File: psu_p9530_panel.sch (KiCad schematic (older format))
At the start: 66 parts, among them IC306 LTC1658, IC308 CD4052B, IC310 TLC272, IC312 TLC272, U401 54LS164

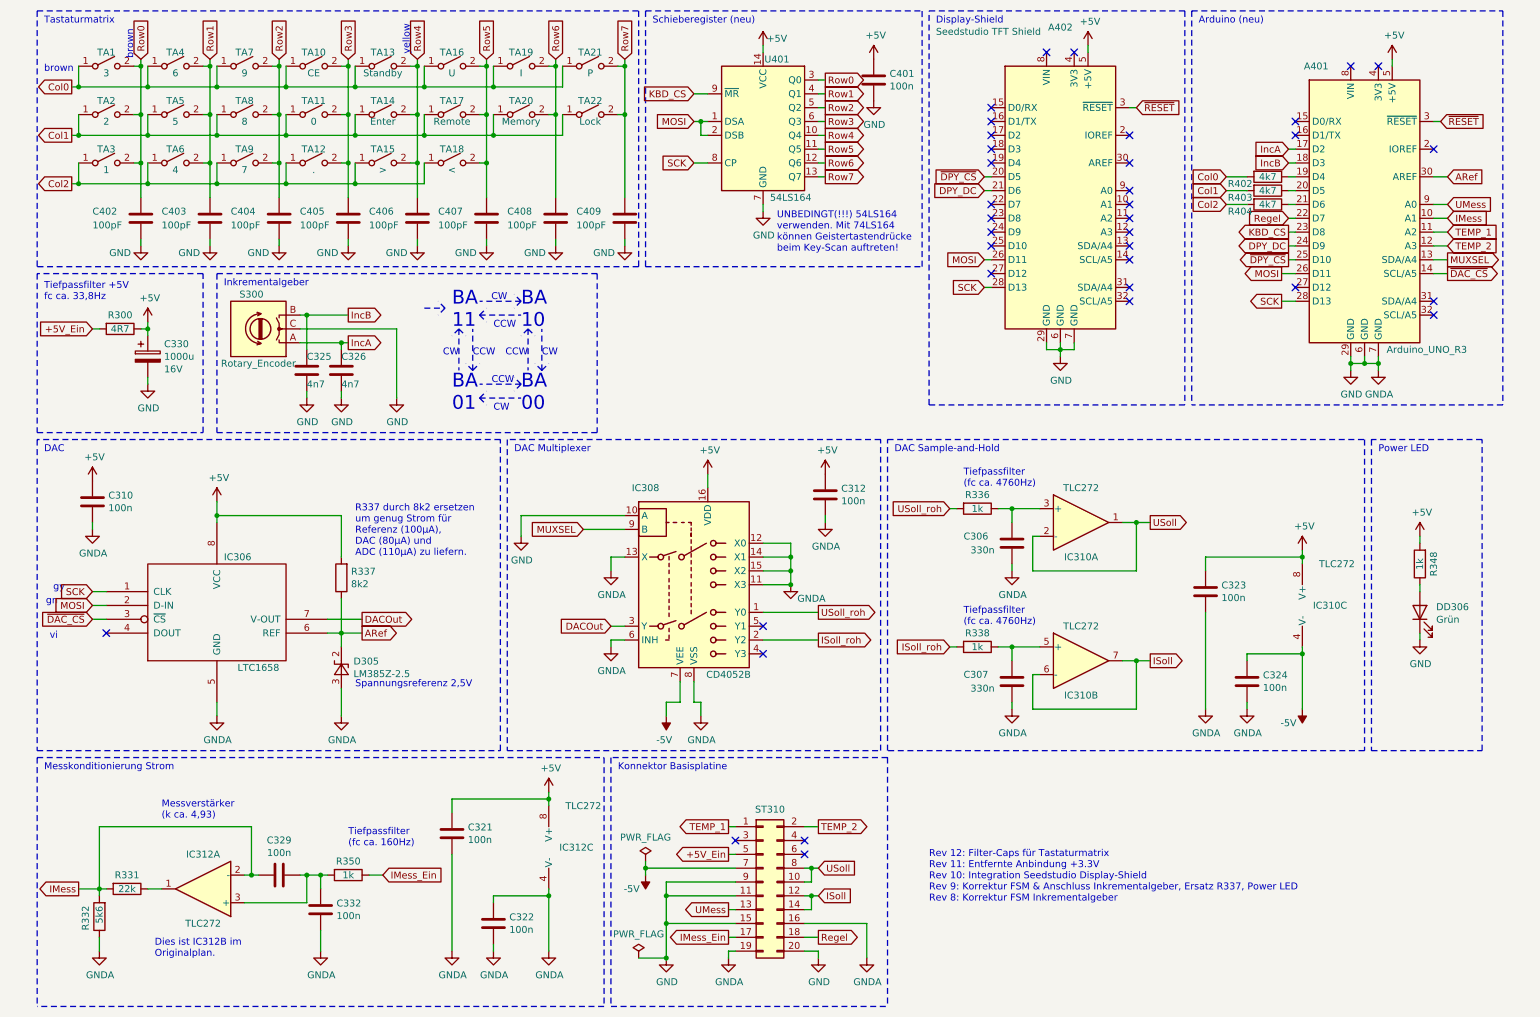
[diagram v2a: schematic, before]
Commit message: Add documentation and translate the schematics
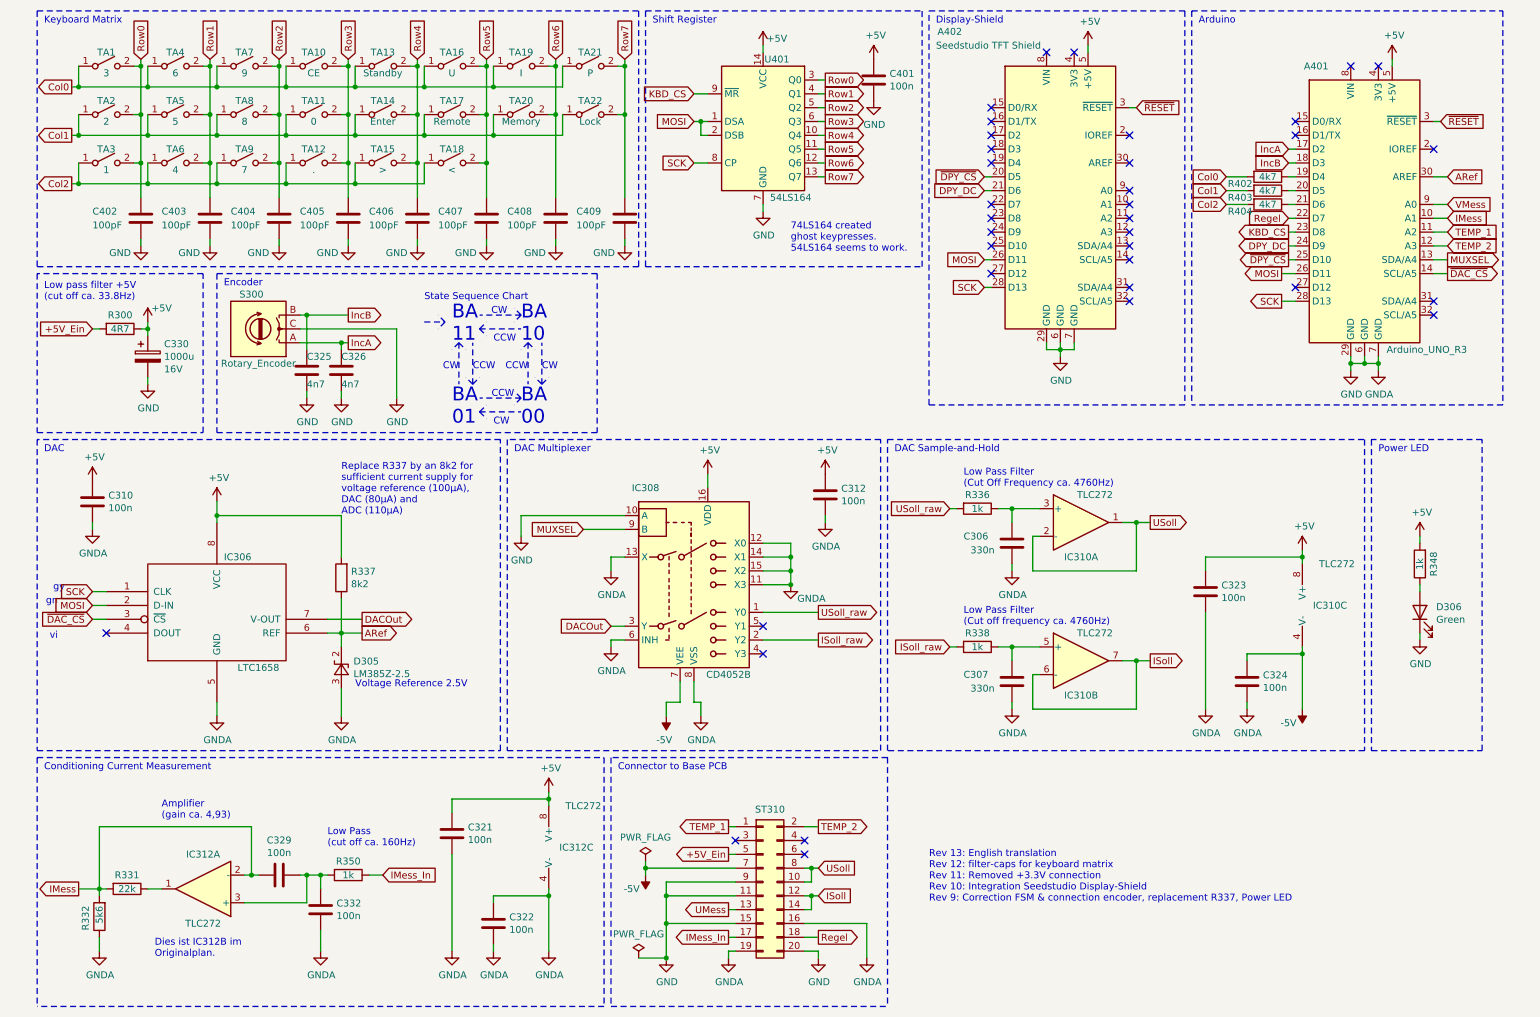
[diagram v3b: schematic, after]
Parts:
- D306: renamed from DD306; value Grün -> Green
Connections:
- net UMess: no longer A401.9 (A0)
- net IMess_Ein renamed IMess_In
- net ISoll_roh renamed ISoll_raw
- net USoll_roh renamed USoll_raw
- new net VMess: A401.9 (A0)
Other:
- note added: "74LS164 created\nghost keypresses.\n54LS164 seems to work."
- note added: "Amplifier\n(gain ca. 4,93)"
- note added: "Arduino"
- note added: "Conditioning Current Measurement"
- note added: "Connector to Base PCB"
- note added: "Encoder"
- note added: "Keyboard Matrix"
- note added: "Low Pass Filter\n(Cut Off Frequency ca. 4760Hz)"
- note added: "Low Pass Filter\n(Cut off frequency ca. 4760Hz)"
- note added: "Low Pass\n(cut off ca. 160Hz)"
- note added: "Low pass filter +5V\n(cut off ca. 33.8Hz)"
- note added: "Replace R337 by an 8k2 for\nsufficient current supply for\nvoltage reference (100µA),\nDAC (80µA) and\nADC (110µA)"
- note added: "Rev 13: English translation\nRev 12: filter-caps for keyboard matrix\nRev 11: Removed +3.3V connection\nRev 10: Integration Seedstudio Display-Shield\nRev 9: Correction FSM & connection encoder, replacement R337, Power LED\n"
- note added: "Shift Register"
- note added: "State Sequence Chart"
- note added: "Voltage Reference 2.5V"
- note removed: "Arduino (neu)"
- note removed: "Inkrementalgeber"
- note removed: "Konnektor Basisplatine"
- note removed: "Messkonditionierung Strom"
- note removed: "Messverstärker\n(k ca. 4,93)"
- note removed: "R337 durch 8k2 ersetzen\num genug Strom für\nReferenz (100µA),\nDAC (80µA) und\nADC (110µA) zu liefern."
- note removed: "Rev 12: Filter-Caps für Tastaturmatrix\nRev 11: Entfernte Anbindung +3.3V\nRev 10: Integration Seedstudio Display-Shield\nRev 9: Korrektur FSM & Anschluss Inkrementalgeber, Ersatz R337, Power LED\nRev 8: Korrektur FSM Inkrementalgeber"
- note removed: "Schieberegister (neu)"
- note removed: "Spannungsreferenz 2,5V"
- note removed: "Tastaturmatrix"
- note removed: "Tiefpassfilter +5V\nfc ca. 33,8Hz"
- note removed: "Tiefpassfilter\n(fc ca. 160Hz)"
- note removed: "Tiefpassfilter\n(fc ca. 4760Hz)"
- note removed: "UNBEDINGT(!!!) 54LS164\nverwenden. Mit 74LS164\nkönnen Geistertastendrücke\nbeim Key-Scan auftreten!"
- note removed: "brown"
- note removed: "yellow"
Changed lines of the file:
@@
 encoding utf-8
 Sheet 1 1
-Title "ELV PS9530 Ersatz Bedienteil"
-Date "2022-09-04"
-Rev "12"
+Title "ELV PS9530 Replacement User Interface"
+Date "2022-11-24"
+Rev "13"
 Comp "Ralf Gerlich"
 Comment1 ""
@@
 UMess
 Text GLabel 5550 7250 0    50   Output ~ 0
-IMess_Ein
+IMess_In
 Text GLabel 6200 7250 2    50   Output ~ 0
 Regel
@@
 	6100 7150 6550 7150
 Text Notes 4750 6050 0    50   ~ 0
-Konnektor Basisplatine
+Connector to Base PCB
 Text GLabel 3050 6800 2    50   Input ~ 0
-IMess_Ein
+IMess_In
 $Comp
 L Device:C C332
@@
 	-1   0    0    1
 $EndComp
-Text Notes 2800 6600 0    50   ~ 0
-Tiefpassfilter\n(fc ca. 160Hz)
+Text Notes 2650 6600 0    50   ~ 0
+Low Pass\n(cut off ca. 160Hz)
 $Comp
 L Device:C C329
@@
 	2100 6800 2050 6800
 Text Notes 1450 6400 0    50   ~ 0
-Messverstärker\n(k ca. 4,93)
+Amplifier\n(gain ca. 4,93)
 Wire Wire Line
 	1350 6900 1450 6900
@@
 	850  6900 1000 6900
 Text Notes 600  6050 0    50   ~ 0
-Messkonditionierung Strom
+Conditioning Current Measurement
 Wire Wire Line
 	6200 7400 6200 7350
@@
 P 8100 4250
 F 0 "IC310" H 8100 4000 50  0000 C CNN
-F 1 "TLC272" H 8100 4500 50  0000 C CNN
+F 1 "TLC272" H 8200 4450 50  0000 C CNN
 F 2 "" H 8100 4250 50  0001 C CNN
 F 3 "http://www.ti.com/lit/ds/symlink/tlc272.pdf" H 8100 4250 50  0001 C CNN
@@
 	7600 4150 7800 4150
 Text GLabel 6200 4900 2    50   Output ~ 0
-USoll_roh
+USoll_raw
 Wire Wire Line
 	6200 4900 5800 4900
 Text GLabel 6200 5100 2    50   Output ~ 0
-ISoll_roh
+ISoll_raw
 Wire Wire Line
 	6200 5100 5800 5100
 Text GLabel 7150 4150 0    50   Input ~ 0
-USoll_roh
+USoll_raw
 Wire Wire Line
 	7150 4150 7200 4150
@@
 P 8100 5250
 F 0 "IC310" H 8100 5000 50  0000 C CNN
-F 1 "TLC272" H 8100 5500 50  0000 C CNN
+F 1 "TLC272" H 8200 5450 50  0000 C CNN
 F 2 "" H 8100 5250 50  0001 C CNN
 F 3 "http://www.ti.com/lit/ds/symlink/tlc272.pdf" H 8100 5250 50  0001 C CNN
@@
 	7600 5150 7800 5150
 Text GLabel 7150 5150 0    50   Input ~ 0
-ISoll_roh
+ISoll_raw
 Wire Wire Line
 	7150 5150 7200 5150
@@
 Connection ~ 1850 4200
 Text Notes 2850 5450 0    50   ~ 0
-Spannungsreferenz 2,5V
+Voltage Reference 2.5V
 Text Notes 4000 3750 0    50   ~ 0
 DAC Multiplexer
@@
 	3900 3650 550  3650
 Text Notes 1900 2550 0    50   ~ 0
-Inkrementalgeber
+Encoder
 NoConn ~ 9650 1350
 NoConn ~ 9650 1450
@@
 	10750 2050 10650 2050
 Text GLabel 10750 1950 2    50   Input ~ 0
-UMess
+VMess
 Wire Wire Line
 	10650 1950 10750 1950
@@
 Col0
 Text Notes 600  650  0    50   ~ 0
-Tastaturmatrix
+Keyboard Matrix
 Text GLabel 9150 1750 0    50   Input ~ 0
 Col0
@@
 MUXSEL
 Text Notes 5000 650  0    50   ~ 0
-Schieberegister (neu)
+Shift Register
 Wire Wire Line
 	5300 1350 5350 1350
@@
 	9600 1950 9650 1950
 Text Notes 8950 650  0    50   ~ 0
-Arduino (neu)
+Arduino
 Wire Notes Line
 	4950 550  6950 550
@@
 P 1350 2800
 F 0 "#PWR0401" H 1350 2650 50  0001 C CNN
-F 1 "+5V" H 1365 2973 50  0000 C CNN
+F 1 "+5V" H 1450 2900 50  0000 C CNN
 F 2 "" H 1350 2800 50  0001 C CNN
 F 3 "" H 1350 2800 50  0001 C CNN
@@
 	1000 2850 950  2850
 Text Notes 600  2650 0    50   ~ 0
-Tiefpassfilter +5V\nfc ca. 33,8Hz
+Low pass filter +5V\n(cut off ca. 33.8Hz)
 Wire Notes Line
 	1750 2450 550  2450
@@
 	1750 3600 1750 2450
 Text Notes 7000 7000 0    50   ~ 0
-Rev 12: Filter-Caps für Tastaturmatrix\nRev 11: Entfernte Anbindung +3.3V\nRev 10: Integration Seedstudio Display-Shield\nRev 9: Korrektur FSM & Anschluss Inkrementalgeber, Ersatz R337, Power LED\nRev 8: Korrektur FSM Inkrementalgeber
+Rev 13: English translation\nRev 12: filter-caps for keyboard matrix\nRev 11: Removed +3.3V connection\nRev 10: Integration Seedstudio Display-Shield\nRev 9: Correction FSM & connection encoder, replacement R337, Power LED\n
 $Comp
 L Device:R R402
@@
 	1    0    0    -1
 $EndComp
-Text Notes 3250 650  3    50   ~ 0
-yellow
-Text Notes 600  1000 0    50   ~ 0
-brown
-Text Notes 4050 2850 0    100  ~ 0
+Text Notes 4050 2950 0    100  ~ 0
 BA\n10
-Text Notes 3550 3450 0    100  ~ 0
+Text Notes 3550 3550 0    100  ~ 0
 BA\n01
 Wire Notes Line
@@
 Wire Notes Line
 	4600 3600 1850 3600
-Text Notes 3550 2850 0    100  ~ 0
+Text Notes 3550 2950 0    100  ~ 0
 BA\n11
 Wire Notes Line style solid
-	3350 2700 3500 2700
-Wire Notes Line style solid
-	3500 2700 3450 2650
-Wire Notes Line style solid
-	3500 2700 3450 2750
+	3350 2800 3500 2800
+Wire Notes Line style solid
+	3500 2800 3450 2750
+Wire Notes Line style solid
+	3500 2800 3450 2850
 $Comp
 L power:-5V #PWR0120
@@
 Text GLabel 9600 1650 0    50   Input ~ 0
 IncB
-Text Notes 2850 4500 0    50   ~ 0
-R337 durch 8k2 ersetzen\num genug Strom für\nReferenz (100µA),\nDAC (80µA) und\nADC (110µA) zu liefern.
+Text Notes 2750 4200 0    50   ~ 0
+Replace R337 by an 8k2 for\nsufficient current supply for\nvoltage reference (100µA),\nDAC (80µA) and\nADC (110µA)
 Text Notes 1400 7400 0    50   ~ 0
 Dies ist IC312B im\nOriginalplan.
@@
 	4900 7400 5100 7400
 Connection ~ 5100 7400
-Text Notes 4050 3450 0    100  ~ 0
+Text Notes 4050 3550 0    100  ~ 0
 BA\n00
-Text Notes 3950 2650 2    50   ~ 0
+Text Notes 3950 2750 2    50   ~ 0
 CW
 Wire Notes Line style solid
-	4050 2650 4000 2600
-Wire Notes Line style solid
-	4050 2650 4000 2700
-Text Notes 3850 2850 0    50   ~ 0
+	4050 2750 4000 2700
+Wire Notes Line style solid
+	4050 2750 4000 2800
+Text Notes 3850 2950 0    50   ~ 0
 CCW
 Wire Notes Line style solid
-	4050 2650 3750 2650
-Wire Notes Line style solid
-	3750 2750 3800 2800
-Wire Notes Line style solid
-	3750 2750 3800 2700
-Wire Notes Line style solid
-	3750 2750 4050 2750
-Text Notes 4200 3050 0    50   ~ 0
+	4050 2750 3750 2750
+Wire Notes Line style solid
+	3750 2850 3800 2900
+Wire Notes Line style solid
+	3750 2850 3800 2800
+Wire Notes Line style solid
+	3750 2850 4050 2850
+Text Notes 4200 3150 0    50   ~ 0
 CW
 Wire Notes Line style solid
-	4200 3150 4250 3100
-Wire Notes Line style solid
-	4200 3150 4150 3100
-Text Notes 4100 3050 2    50   ~ 0
+	4200 3250 4250 3200
+Wire Notes Line style solid
+	4200 3250 4150 3200
+Text Notes 4100 3150 2    50   ~ 0
 CCW
 Wire Notes Line style solid
-	4200 3150 4200 2850
-Wire Notes Line style solid
-	4100 2850 4050 2900
-Wire Notes Line style solid
-	4100 2850 4150 2900
-Wire Notes Line style solid
-	4100 2850 4100 3150
-Text Notes 3850 3450 0    50   ~ 0
+	4200 3250 4200 2950
+Wire Notes Line style solid
+	4100 2950 4050 3000
+Wire Notes Line style solid
+	4100 2950 4150 3000
+Wire Notes Line style solid
+	4100 2950 4100 3250
+Text Notes 3850 3550 0    50   ~ 0
 CW
 Wire Notes Line style solid
-	3750 3350 3800 3400
-Wire Notes Line style solid
-	3750 3350 3800 3300
-Text Notes 4000 3250 2    50   ~ 0
+	3750 3450 3800 3500
+Wire Notes Line style solid
+	3750 3450 3800 3400
+Text Notes 4000 3350 2    50   ~ 0
 CCW
 Wire Notes Line style solid
-	3750 3350 4050 3350
-Wire Notes Line style solid
-	4050 3250 4000 3200
-Wire Notes Line style solid
-	4050 3250 4000 3300
-Wire Notes Line style solid
-	4050 3250 3750 3250
-Text Notes 3600 3050 2    50   ~ 0
+	3750 3450 4050 3450
+Wire Notes Line style solid
+	4050 3350 4000 3300
+Wire Notes Line style solid
+	4050 3350 4000 3400
+Wire Notes Line style solid
+	4050 3350 3750 3350
+Text Notes 3600 3150 2    50   ~ 0
 CW
 Wire Notes Line style solid
-	3600 2850 3550 2900
-Wire Notes Line style solid
-	3600 2850 3650 2900
-Text Notes 3700 3050 0    50   ~ 0
+	3600 2950 3550 3000
+Wire Notes Line style solid
+	3600 2950 3650 3000
+Text Notes 3700 3150 0    50   ~ 0
 CCW
 Wire Notes Line style solid
-	3600 2850 3600 3150
-Wire Notes Line style solid
-	3700 3150 3750 3100
-Wire Notes Line style solid
-	3700 3150 3650 3100
-Wire Notes Line style solid
-	3700 3150 3700 2850
+	3600 2950 3600 3250
+Wire Notes Line style solid
+	3700 3250 3750 3200
+Wire Notes Line style solid
+	3700 3250 3650 3200
+Wire Notes Line style solid
+	3700 3250 3700 2950
 Text Notes 7250 4000 0    50   ~ 0
-Tiefpassfilter\n(fc ca. 4760Hz)
+Low Pass Filter\n(Cut Off Frequency ca. 4760Hz)
 Text Notes 7250 5000 0    50   ~ 0
-Tiefpassfilter\n(fc ca. 4760Hz)
+Low Pass Filter\n(Cut off frequency ca. 4760Hz)
 $Comp
 L power:+5V #PWR0129
@@
 $EndComp
 $Comp
-L Device:LED DD306
+L Device:LED D306
 U 1 1 6349C312
 P 10550 4900
-F 0 "DD306" V 10589 4782 50  0000 R CNN
-F 1 "Grün" V 10498 4782 50  0000 R CNN
+F 0 "D306" V 10589 4782 50  0000 R CNN
+F 1 "Green" V 10498 4782 50  0000 R CNN
 F 2 "" H 10550 4900 50  0001 C CNN
 F 3 "~" H 10550 4900 50  0001 C CNN
@@
 U 1 1 6312D27C
 P 7950 1850
-F 0 "A402" H 7950 3031 50  0000 C CNN
-F 1 "Seedstudio TFT Shield" H 7050 3000 50  0000 L CNN
+F 0 "A402" H 7150 3000 50  0000 C CNN
+F 1 "Seedstudio TFT Shield" H 7050 2900 50  0000 L CNN
 F 2 "Module:Arduino_UNO_R3" H 7950 1850 50  0001 C CIN
 F 3 "https://www.arduino.cc/en/Main/arduinoBoardUno" H 7950 1850 50  0001 C CNN
@@
 Wire Notes Line
 	8850 550  7000 550
-Text Notes 5900 2300 0    50   ~ 0
-UNBEDINGT(!!!) 54LS164\nverwenden. Mit 74LS164\nkönnen Geistertastendrücke\nbeim Key-Scan auftreten!
+Text Notes 6000 2300 0    50   ~ 0
+74LS164 created\nghost keypresses.\n54LS164 seems to work.
 $Comp
 L 74xx:74HCT164 U401
@@
 	1    0    0    -1
 $EndComp
-Text Notes 1250 900  1    50   ~ 0
-brown
 $Comp
 L Switch:SW_SPST TA4
@@
 Wire Wire Line
 	4300 1300 4300 1900
+Text Notes 3350 2650 0    50   ~ 0
+State Sequence Chart
 $EndSCHEMATC
